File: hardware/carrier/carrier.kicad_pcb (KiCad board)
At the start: 2 copper layers, 46 x 46 mm, 10 parts, among them J1 Display H2, J2 CAN SN65HVD230, J3 GNSS GY-GPSV3, J4 Buck OUT, J5 OBD cable, J6 Rs wire pad, J7 Buck IN+ wire pad

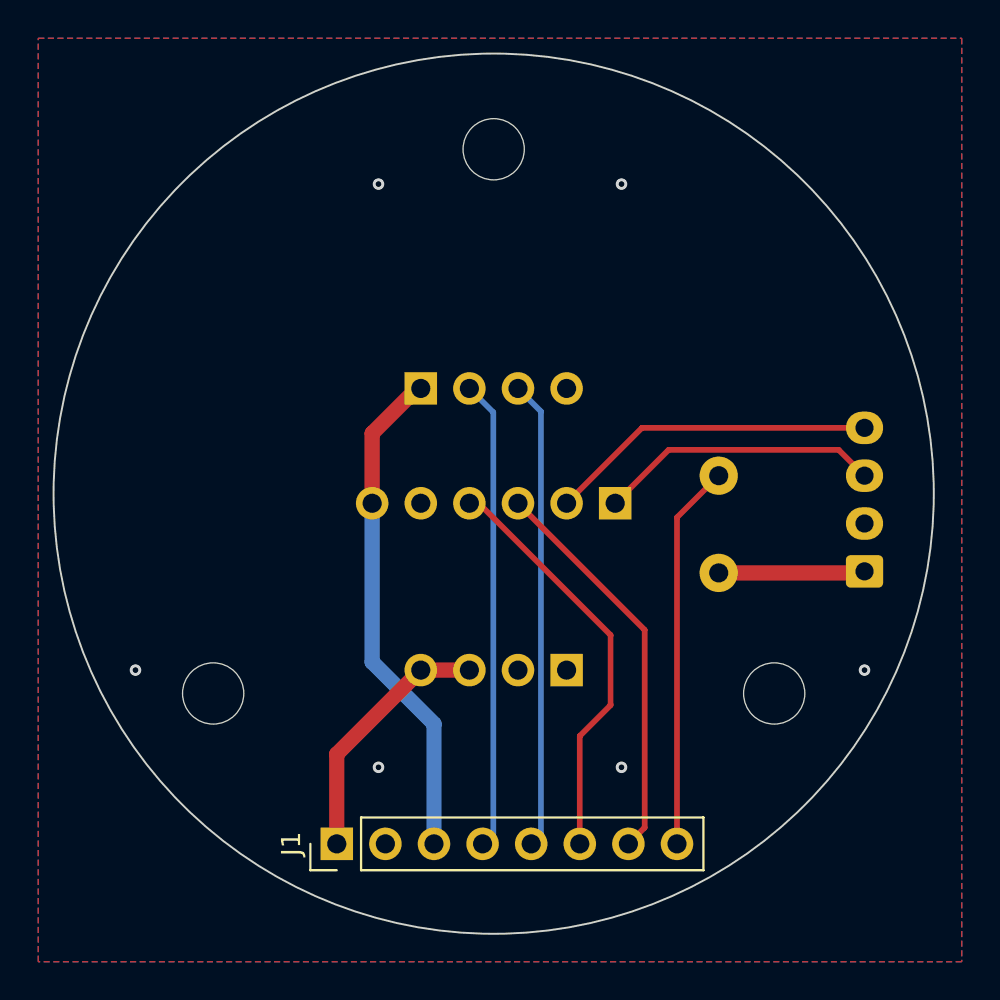
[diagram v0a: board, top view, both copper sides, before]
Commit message: Carrier: J1 1 mm left, and the parts named on the silkscreen
The display's header sat 1 mm too far right: J1 is now at -9.20 mm
from the centre (front view), its eight tracks re-routed from the pads
up to their first bend, and the GND pour refilled. gen_pcb.py's
J1_PIN1 and the board's note say so.

The back now says what goes where: the display's H2 pin names over
J1's pads (5V GND 3V3 IO43 IO44 IO16 IO17 IO18), and every part by
name instead of its J number - DISPLAY, GNSS, CAN, BUCK, OBD, CAN Rs,
BUCK IN+. The references are only hidden, so the schematic still
matches. Four names sit away from where the reference was, which
collided or ran off the edge. DRC: no new violations.
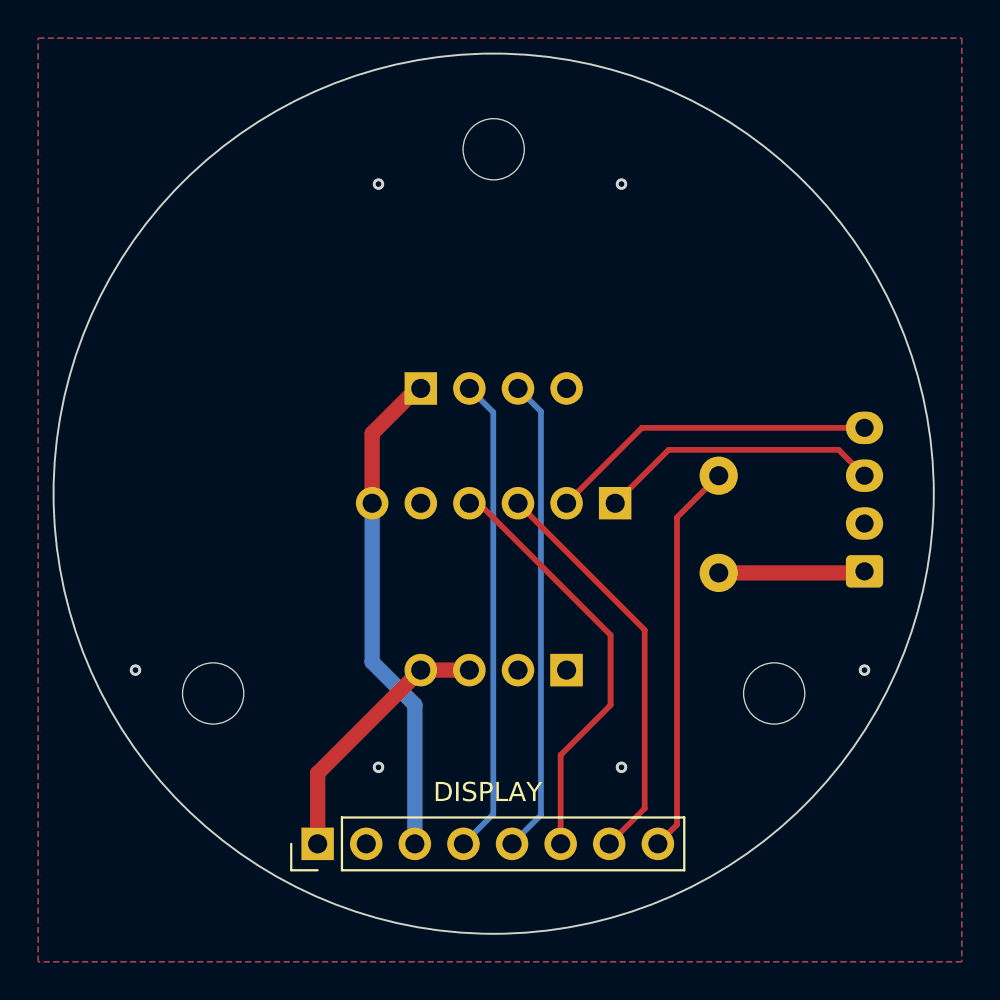
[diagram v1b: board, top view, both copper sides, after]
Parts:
- moved J1 1.00 mm to (90.8, 118.3)
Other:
- board text added: "5V"
- board text added: "IO16"
- board text added: "IO17"
- board text added: "IO18"
- board text added: "IO43"
- board text added: "IO44"
- board text added: "J1 verified against the display (calipers, 2026-09-30), then moved 1 mm left (2026-10-15)"
- board text removed: "J1 position verified against the display (calipers, 2026-09-30)"
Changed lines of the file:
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@@
 	(footprint "PinHeader_1x08_P2.54mm_Vertical"
 		(layer "F.Cu")
-		(at 91.8 118.3 90)
+		(at 90.8 118.3 90)
 		(descr "Through hole straight pin header, 1x08, 2.54mm pitch, single row")
 		(tags "Through hole pin header THT 1x08 2.54mm single row")
+		(fp_text user "DISPLAY"
+			(at 2.7 8.89 0)
+			(layer "F.SilkS")
+			(effects
+				(font
+					(size 1 1)
+					(thickness 0.15)
+				)
+			)
+		)
 		(property "Reference" "J1"
 			(at 0 -2.38 90)
 			(layer "F.SilkS")
+			(hide yes)
 			(effects
 				(font
@@
 		(descr "JST XH series connector, B4B-XH-A (http://www.jst-mfg.com/product/pdf/eng/eXH.pdf)")
 		(tags "connector JST XH vertical")
+		(fp_text user "OBD"
+			(at 11.46 0.12 0)
+			(layer "B.SilkS")
+			(effects
+				(font
+					(size 1 1)
+					(thickness 0.15)
+				)
+				(justify mirror)
+			)
+		)
 		(property "Reference" "J5"
 			(at 3.75 3.55 90)
 			(layer "B.SilkS")
+			(hide yes)
 			(effects
 				(font
@@
 		(descr "THT pad as test Point, diameter 2.0mm, hole diameter 1.0mm")
 		(tags "test point THT pad")
+		(fp_text user "CAN Rs"
+			(at 0 1.998 0)
+			(layer "B.SilkS")
+			(effects
+				(font
+					(size 1 1)
+					(thickness 0.15)
+				)
+				(justify mirror)
+			)
+		)
 		(property "Reference" "J6"
 			(at 0 1.998 0)
 			(layer "B.SilkS")
+			(hide yes)
 			(effects
 				(font
@@
 		(descr "Through hole straight socket strip, 1x04, 2.54mm pitch, single row (from Kicad 4.0.7), script generated")
 		(tags "Through hole socket strip THT 1x04 2.54mm single row")
+		(fp_text user "GNSS"
+			(at 0 2.77 90)
+			(layer "B.SilkS")
+			(effects
+				(font
+					(size 1 1)
+					(thickness 0.15)
+				)
+				(justify mirror)
+			)
+		)
 		(property "Reference" "J3"
 			(at 0 2.77 90)
 			(layer "B.SilkS")
+			(hide yes)
 			(effects
 				(font
@@
 		(descr "Through hole straight socket strip, 1x06, 2.54mm pitch, single row (from Kicad 4.0.7), script generated")
 		(tags "Through hole socket strip THT 1x06 2.54mm single row")
+		(fp_text user "CAN"
+			(at 0 -15.05 90)
+			(layer "B.SilkS")
+			(effects
+				(font
+					(size 1 1)
+					(thickness 0.15)
+				)
+				(justify mirror)
+			)
+		)
 		(property "Reference" "J2"
 			(at 0 2.77 90)
 			(layer "B.SilkS")
+			(hide yes)
 			(effects
 				(font
@@
 		(descr "Through hole straight socket strip, 1x04, 2.54mm pitch, single row (from Kicad 4.0.7), script generated")
 		(tags "Through hole socket strip THT 1x04 2.54mm single row")
+		(fp_text user "BUCK"
+			(at 0 2.77 90)
+			(layer "B.SilkS")
+			(effects
+				(font
+					(size 1 1)
+					(thickness 0.15)
+				)
+				(justify mirror)
+			)
+		)
 		(property "Reference" "J4"
 			(at 0 2.77 90)
 			(layer "B.SilkS")
+			(hide yes)
 			(effects
 				(font
@@
 		(descr "THT pad as test Point, diameter 2.0mm, hole diameter 1.0mm")
 		(tags "test point THT pad")
+		(fp_text user "BUCK IN+"
+			(at 0 -2.15 0)
+			(layer "B.SilkS")
+			(effects
+				(font
+					(size 1 1)
+					(thickness 0.15)
+				)
+				(justify mirror)
+			)
+		)
 		(property "Reference" "J7"
 			(at 0 1.998 0)
 			(layer "B.SilkS")
+			(hide yes)
 			(effects
 				(font
@@
 		)
 	)
+	(gr_text "5V"
+		(at 90.8 117.25 90)
+		(layer "B.SilkS")
+		(effects
+			(font
+				(size 0.8 0.8)
+				(thickness 0.12)
+			)
+			(justify right mirror)
+		)
+	)
+	(gr_text "GND"
+		(at 93.34 117.25 90)
+		(layer "B.SilkS")
+		(effects
+			(font
+				(size 0.8 0.8)
+				(thickness 0.12)
+			)
+			(justify right mirror)
+		)
+	)
+	(gr_text "3V3"
+		(at 95.88 117.25 90)
+		(layer "B.SilkS")
+		(effects
+			(font
+				(size 0.8 0.8)
+				(thickness 0.12)
+			)
+			(justify right mirror)
+		)
+	)
+	(gr_text "IO43"
+		(at 98.42 117.25 90)
+		(layer "B.SilkS")
+		(effects
+			(font
+				(size 0.8 0.8)
+				(thickness 0.12)
+			)
+			(justify right mirror)
+		)
+	)
+	(gr_text "IO44"
+		(at 100.96 117.25 90)
+		(layer "B.SilkS")
+		(effects
+			(font
+				(size 0.8 0.8)
+				(thickness 0.12)
+			)
+			(justify right mirror)
+		)
+	)
+	(gr_text "IO16"
+		(at 103.5 117.25 90)
+		(layer "B.SilkS")
+		(effects
+			(font
+				(size 0.8 0.8)
+				(thickness 0.12)
+			)
+			(justify right mirror)
+		)
+	)
+	(gr_text "IO17"
+		(at 106.04 117.25 90)
+		(layer "B.SilkS")
+		(effects
+			(font
+				(size 0.8 0.8)
+				(thickness 0.12)
+			)
+			(justify right mirror)
+		)
+	)
+	(gr_text "IO18"
+		(at 108.58 117.25 90)
+		(layer "B.SilkS")
+		(effects
+			(font
+				(size 0.8 0.8)
+				(thickness 0.12)
+			)
+			(justify right mirror)
+		)
+	)
 	(gr_text "GNSS 27x4"
 		(at 89.5 91.6 0)
@@
 		)
 	)
-	(gr_text "J1 position verified against the display (calipers, 2026-09-30)"
+	(gr_text "J1 verified against the display (calipers, 2026-09-30), then moved 1 mm left (2026-10-15)"
 		(at 100 74 0)
 		(layer "Cmts.User")
@@
 	)
 	(segment
-		(start 91.8 118.3)
-		(end 91.8 113.61)
+		(start 90.8 118.3)
+		(end 90.8 114.61)
 		(width 0.8)
 		(layer "F.Cu")
@@
 	)
 	(segment
-		(start 91.8 113.61)
+		(start 90.8 114.61)
 		(end 96.19 109.22)
 		(width 0.8)
@@
 	)
 	(segment
-		(start 96.88 112.031321)
+		(start 95.88 111.031321)
 		(end 93.65 108.801321)
 		(width 0.8)
@@
 	)
 	(segment
-		(start 96.88 118.3)
-		(end 96.88 112.031321)
+		(start 95.88 118.3)
+		(end 95.88 111.031321)
 		(width 0.8)
 		(layer "B.Cu")
@@
 	)
 	(segment
-		(start 99.98 117.74)
+		(start 99.98 116.74)
 		(end 99.98 95.75)
 		(width 0.3)
@@
 	)
 	(segment
-		(start 99.42 118.3)
-		(end 99.98 117.74)
+		(start 98.42 118.3)
+		(end 99.98 116.74)
 		(width 0.3)
 		(layer "B.Cu")
@@
 	)
 	(segment
-		(start 102.47 117.79)
+		(start 102.47 116.79)
 		(end 102.47 95.7)
 		(width 0.3)
@@
 	)
 	(segment
-		(start 101.96 118.3)
-		(end 102.47 117.79)
+		(start 100.96 118.3)
+		(end 102.47 116.79)
 		(width 0.3)
 		(layer "B.Cu")
@@
 	)
 	(segment
-		(start 104.5 112.661371)
+		(start 103.5 113.661371)
 		(end 106.11 111.051371)
 		(width 0.3)
@@
 	)
 	(segment
-		(start 104.5 118.3)
-		(end 104.5 112.661371)
+		(start 103.5 118.3)
+		(end 103.5 113.661371)
 		(width 0.3)
 		(layer "F.Cu")
@@
 	)
 	(segment
-		(start 107.04 118.3)
-		(end 107.89 117.45)
+		(start 106.04 118.3)
+		(end 107.89 116.45)
 		(width 0.3)
 		(layer "F.Cu")
@@
 	)
 	(segment
-		(start 107.89 117.45)
+		(start 107.89 116.45)
 		(end 107.89 107.12)
 		(width 0.3)
@@
 	)
 	(segment
-		(start 109.58 118.3)
+		(start 108.58 118.3)
+		(end 109.58 117.3)
+		(width 0.3)
+		(layer "F.Cu")
+		(net "CAN_RS")
+	)
+	(segment
+		(start 109.58 117.3)
 		(end 109.58 101.24)
 		(width 0.3)
